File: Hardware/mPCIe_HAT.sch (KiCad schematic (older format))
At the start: 105 parts, among them K1 USB_C_Receptacle_USB2.0, M1 MPCIE_LATCH, Q2 BC856BS, Q3 DMP3013SFV

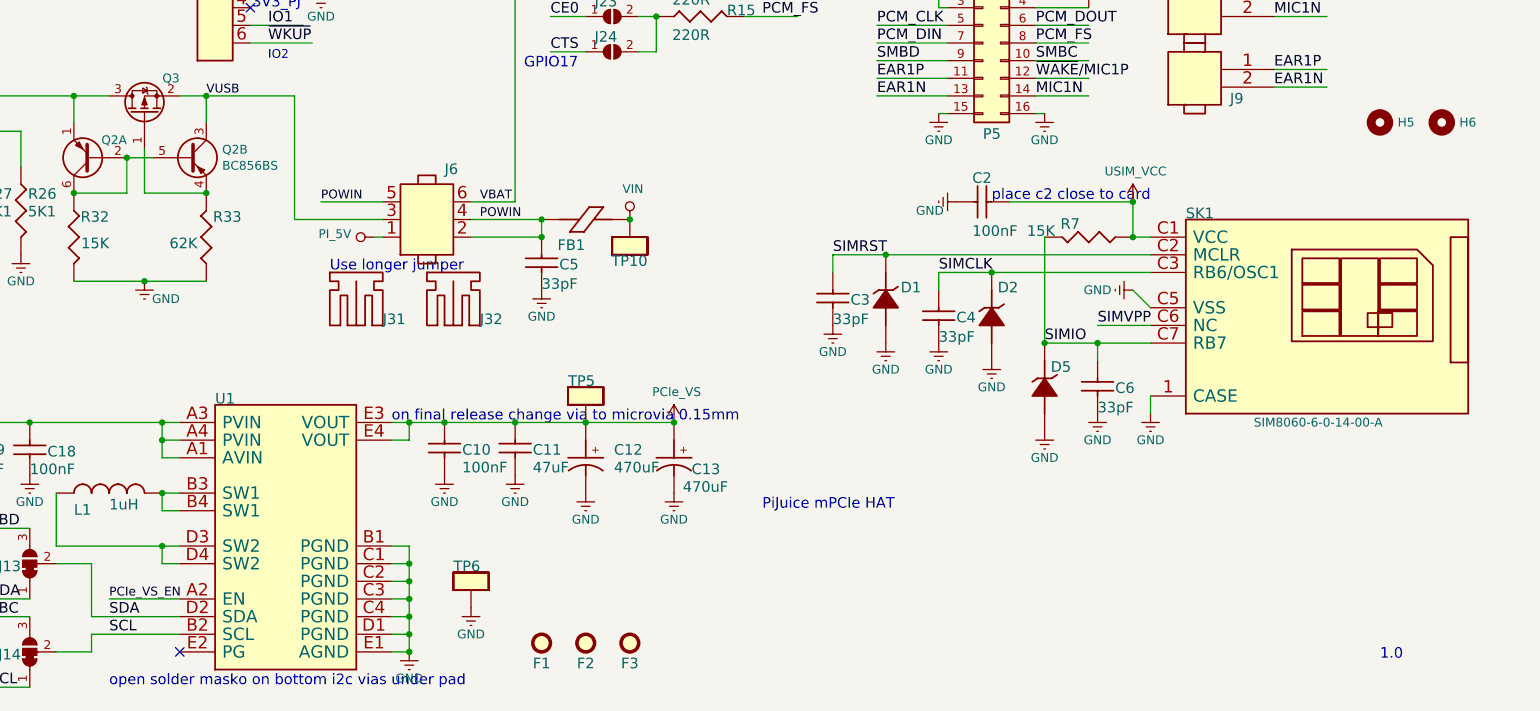
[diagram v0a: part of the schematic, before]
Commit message: Q2B connection fix, position file generated.
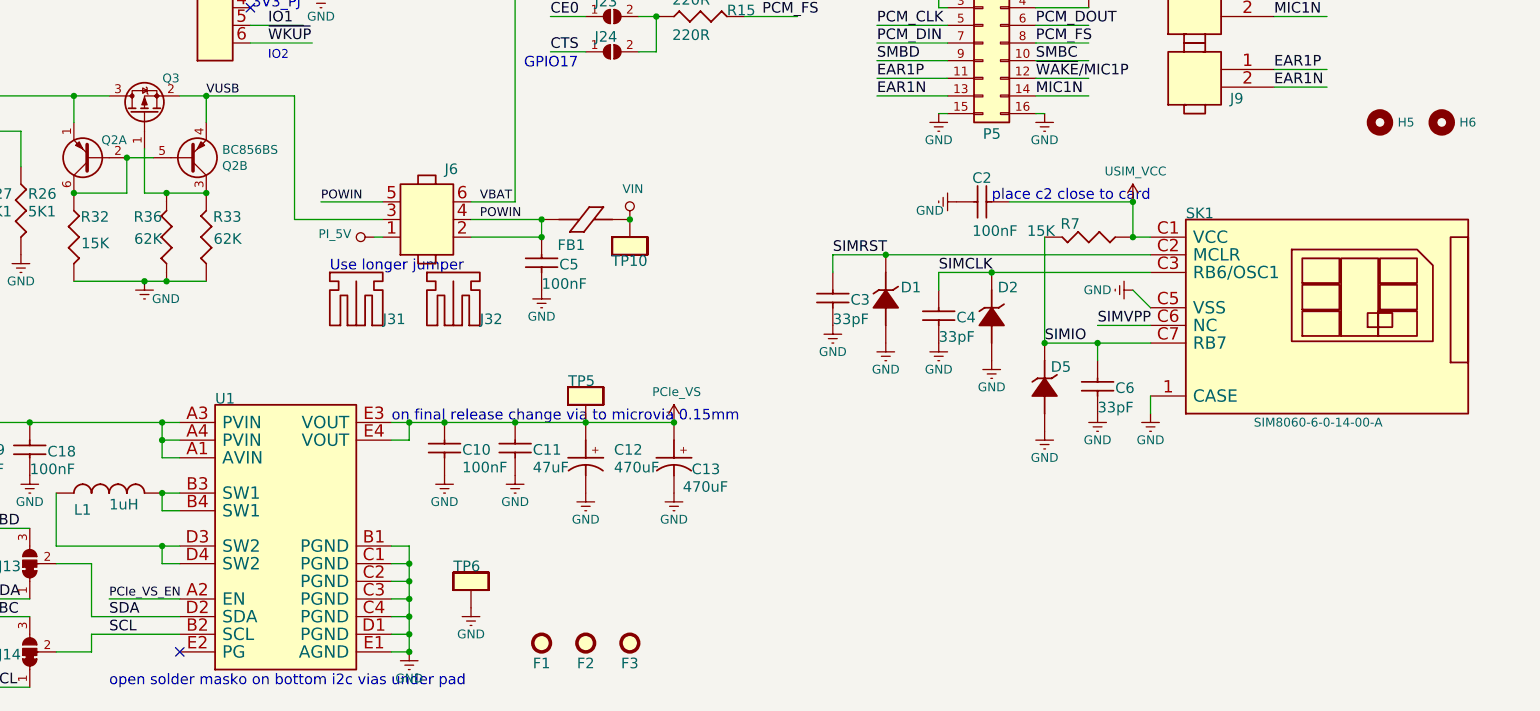
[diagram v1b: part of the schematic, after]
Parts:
- added R36: 62K, Resistor_SMD:R_0402_1005Metric, symbol mPCIe_HAT-SchLib:R-
- C5: value 33pF -> 100nF; Manufacturer Yageo -> 100nF; Part Number CC0402JRNP09BN330 -> GRM155R61E104KA87D
- FB1: Manufacturer Laird Technologies -> Taiyo Yuden; Part Number HI1206T500R-10 -> FBMJ3216HS480NT
- P3: Alternative Manufacturer (none) -> E-tec; Alternative Manufacturer Alternative E-tec -> (none)
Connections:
- wire segments 305 -> 307
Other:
- note removed: "1.0"
- note removed: "PiJuice mPCIe HAT"
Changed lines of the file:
@@
 encoding utf-8
 Sheet 1 2
-Title "mPCIe_HAT-SchDoc"
-Date "09 02 2021"
-Rev ""
-Comp ""
+Title "PiJuice mPCIe HAT"
+Date "2021-12-30"
+Rev "1.1"
+Comp "Nebra Ltd"
 Comment1 ""
 Comment2 ""
@@
 Text Label 7100 1300 0    60   ~ 0
 EAR1N
-Text Notes 6450 7000 0    60   ~ 0
-PiJuice mPCIe HAT
-Text Notes 9950 7850 0    60   ~ 0
-1.0
 Text Notes 4350 6500 0    60   ~ 0
 on final release change via to microvia 0.15mm
@@
 F 5 "NEXPERIA" H 3200 5000 50  0001 C CNN "Manufacturer"
 	2    3200 5000
-	1    0    0    -1
+	1    0    0    1
 $EndComp
 $Comp
@@
 P 3300 5700
 F 0 "R33" V 3700 5500 60  0000 L BNN
-F 1 "62K" V 3550 5750 60  0000 L BNN
+F 1 "62K" V 3575 5500 60  0000 L BNN
 F 2 "Resistor_SMD:R_0402_1005Metric" H 3700 5700 60  0001 C CNN
 F 3 "" H 3700 5700 60  0001 C CNN
@@
 Connection ~ 2950 5700
 Wire Wire Line
-	2950 5700 3300 5700
+	2950 5700 3075 5700
 Wire Wire Line
 	2850 5000 3000 5000
@@
 $EndComp
 Wire Wire Line
-	3300 5200 2950 5200
+	3300 5200 3075 5200
 Wire Wire Line
 	2950 5200 2950 4950
@@
 F 5 "GCT" H 3450 3750 50  0001 C CNN "Manufacturer"
 F 6 "BS1-006-H500-55/B" H 3450 3750 50  0001 C CNN "Alternative"
-F 7 "E-tec" H 3450 3750 50  0001 C CNN "Alternative Manufacturer Alternative"
+F 7 "E-tec" H 3450 3750 50  0001 C CNN "Alternative Manufacturer"
 	1    3450 3750
 	-1   0    0    -1
@@
 P 5100 5550
 F 0 "C5" H 5300 5460 60  0000 L BNN
-F 1 "33pF" H 5200 5350 60  0000 L BNN
+F 1 "100nF" H 5200 5350 60  0000 L BNN
 F 2 "Capacitor_SMD:C_0402_1005Metric" H 5200 5350 60  0001 C CNN
 F 3 "" H 5200 5350 60  0001 C CNN
-F 4 "Yageo" H 5100 5550 50  0001 C CNN "Manufacturer"
-F 5 "CC0402JRNP09BN330" H 5100 5550 50  0001 C CNN "Part Number"
+F 4 "100nF" H 5100 5550 50  0001 C CNN "Manufacturer"
+F 5 "GRM155R61E104KA87D" H 5100 5550 50  0001 C CNN "Part Number"
 	1    5100 5550
 	1    0    0    -1
@@
 F 2 "PiJuice_mPCIe_HAT_PcbLib:FBD_1206_3216Metric" H 5700 5350 50  0001 C CNN
 F 3 "" H 5700 5350 50  0001 C CNN
-F 4 "Laird Technologies" H 5700 5350 50  0001 C CNN "Manufacturer"
-F 5 "HI1206T500R-10" H 5700 5350 50  0001 C CNN "Part Number"
+F 4 "Taiyo Yuden" H 5700 5350 50  0001 C CNN "Manufacturer"
+F 5 "FBMJ3216HS480NT" H 5700 5350 50  0001 C CNN "Part Number"
 	1    5700 5350
 	-1   0    0    1
@@
 	0    1    1    0
 $EndComp
+$Comp
+L mPCIe_HAT-SchLib:R- R36
+U 1 1 6101A65B
+P 3075 5700
+F 0 "R36" V 3475 5725 60  0000 L BNN
+F 1 "62K" V 3350 5725 60  0000 L BNN
+F 2 "Resistor_SMD:R_0402_1005Metric" H 3475 5700 60  0001 C CNN
+F 3 "" H 3475 5700 60  0001 C CNN
+F 4 "Yageo" H 3075 5700 50  0001 C CNN "Manufacturer"
+F 5 "RC0402FR-0762KL" H 3075 5700 50  0001 C CNN "Part Number"
+	1    3075 5700
+	0    -1   -1   0
+$EndComp
+Connection ~ 3075 5700
+Wire Wire Line
+	3075 5700 3300 5700
+Connection ~ 3075 5200
+Wire Wire Line
+	3075 5200 2950 5200
 $EndSCHEMATC
